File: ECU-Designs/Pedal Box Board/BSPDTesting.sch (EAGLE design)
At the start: 18 parts, among them X1 MINIFIT_5566-2

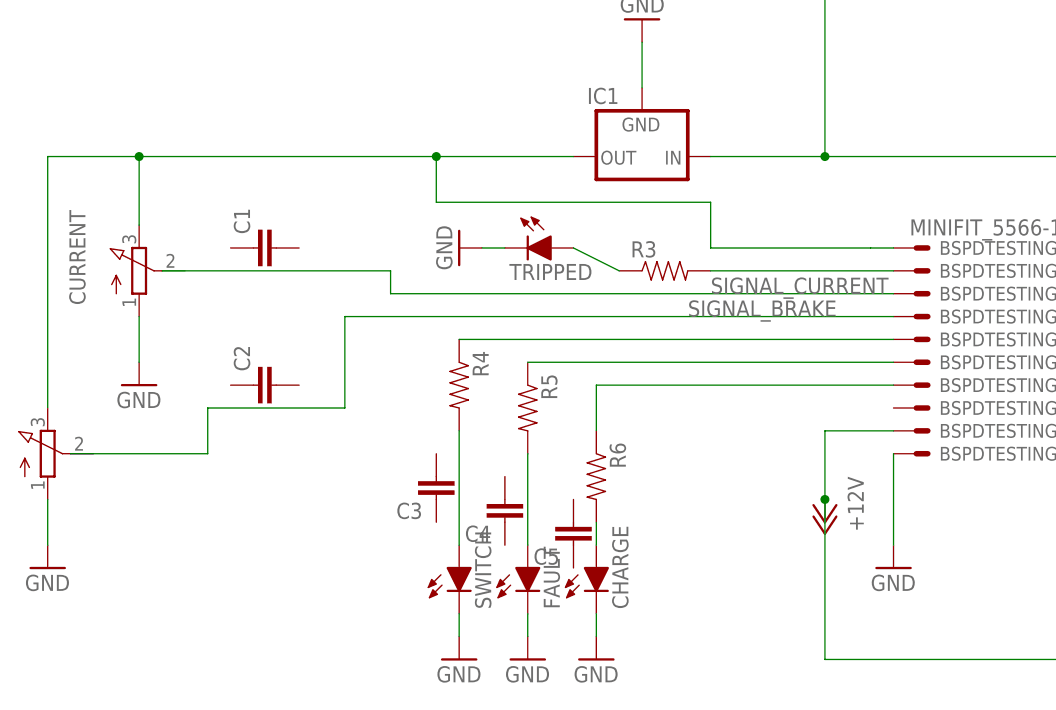
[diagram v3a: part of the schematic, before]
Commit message: Added Test Points to the library (usable with probes) updated board  to accomodate Test Probes.
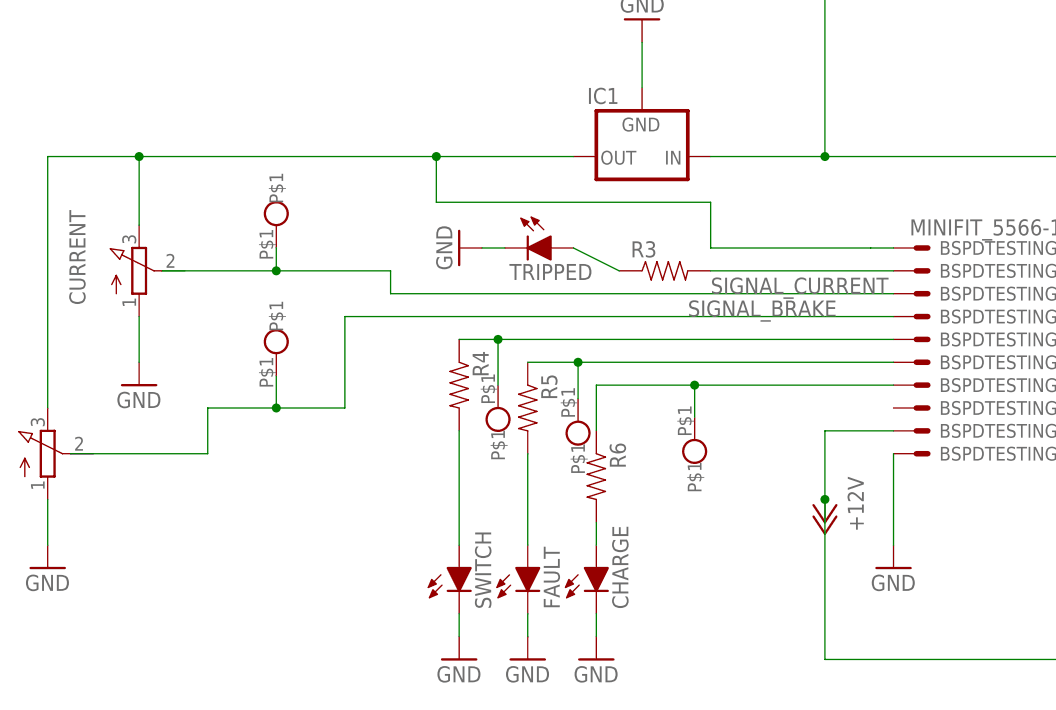
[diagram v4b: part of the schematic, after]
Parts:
- removed C1, C2, C3, C4, C5: (no value), HyTechDevices:CAPEZ
- added BRAKEPROBE, CURRENTPROBE, U$3, U$4, U$5: TEST_POINT_COMPACT_THM, HyTechDevices:TEST_POINT_COMPACT_THM
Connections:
- net N$10: now also U$4.P$1
- net N$14: now also U$5.P$1
- net N$9: now also U$3.P$1
- net SIGNAL_BRAKE: now also BRAKEPROBE.P$1
- net SIGNAL_CURRENT: now also CURRENTPROBE.P$1
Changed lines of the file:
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@@
 <setting verticaltext="up"/>
 </settings>
-<grid distance="0.1" unitdist="inch" unit="inch" style="lines" multiple="1" display="no" altdistance="0.01" altunitdist="inch" altunit="inch"/>
+<grid distance="0.01" unitdist="inch" unit="inch" style="lines" multiple="1" display="no" altdistance="0.01" altunitdist="inch" altunit="inch"/>
 <layers>
 <layer number="1" name="Top" color="4" fill="1" visible="no" active="no"/>
@@
 <part name="X1" library="HyTechDevices" deviceset="MINIFIT_5566-2" device=""/>
 <part name="GND9" library="supply1" deviceset="GND" device=""/>
-<part name="C1" library="HyTechDevices" deviceset="CAP" device="EZ"/>
-<part name="C2" library="HyTechDevices" deviceset="CAP" device="EZ"/>
-<part name="C3" library="HyTechDevices" deviceset="CAP" device="EZ"/>
-<part name="C4" library="HyTechDevices" deviceset="CAP" device="EZ"/>
-<part name="C5" library="HyTechDevices" deviceset="CAP" device="EZ"/>
+<part name="BRAKEPROBE" library="HyTechDevices" deviceset="TEST_POINT_COMPACT_THM" device=""/>
+<part name="CURRENTPROBE" library="HyTechDevices" deviceset="TEST_POINT_COMPACT_THM" device=""/>
+<part name="U$3" library="HyTechDevices" deviceset="TEST_POINT_COMPACT_THM" device=""/>
+<part name="U$4" library="HyTechDevices" deviceset="TEST_POINT_COMPACT_THM" device=""/>
+<part name="U$5" library="HyTechDevices" deviceset="TEST_POINT_COMPACT_THM" device=""/>
 </parts>
 <sheets>
@@
 <instance part="X1" gate="-1" x="96.52" y="104.14" rot="R90"/>
 <instance part="GND9" gate="1" x="96.52" y="99.06"/>
-<instance part="C1" gate="G$1" x="45.72" y="60.96" rot="R90"/>
-<instance part="C2" gate="G$1" x="45.72" y="45.72" rot="R90"/>
-<instance part="C3" gate="G$1" x="63.5" y="35.56" rot="R180"/>
-<instance part="C4" gate="G$1" x="71.12" y="33.02" rot="R180"/>
-<instance part="C5" gate="G$1" x="78.74" y="30.48" rot="R180"/>
+<instance part="BRAKEPROBE" gate="G$1" x="45.72" y="50.546" rot="R90"/>
+<instance part="CURRENTPROBE" gate="G$1" x="45.72" y="64.77" rot="R90"/>
+<instance part="U$3" gate="G$1" x="70.358" y="41.91" rot="R270"/>
+<instance part="U$4" gate="G$1" x="79.248" y="40.386" rot="R270"/>
+<instance part="U$5" gate="G$1" x="92.202" y="38.354" rot="R270"/>
 </instances>
 <busses>
@@
 <wire x1="22.86" y1="38.1" x2="38.1" y2="38.1" width="0.1524" layer="91"/>
 <wire x1="38.1" y1="38.1" x2="38.1" y2="43.18" width="0.1524" layer="91"/>
-<wire x1="53.34" y1="43.18" x2="38.1" y2="43.18" width="0.1524" layer="91"/>
+<wire x1="53.34" y1="43.18" x2="45.72" y2="43.18" width="0.1524" layer="91"/>
+<pinref part="BRAKEPROBE" gate="G$1" pin="P$1"/>
+<wire x1="45.72" y1="43.18" x2="38.1" y2="43.18" width="0.1524" layer="91"/>
+<wire x1="45.72" y1="46.736" x2="45.72" y2="43.18" width="0.1524" layer="91"/>
+<junction x="45.72" y="43.18"/>
 </segment>
 </net>
@@
 <pinref part="R4" gate="G$1" pin="1"/>
 <pinref part="BSPDTESTING" gate="-5" pin="S"/>
-<wire x1="66.04" y1="50.8" x2="114.3" y2="50.8" width="0.1524" layer="91"/>
+<wire x1="66.04" y1="50.8" x2="70.358" y2="50.8" width="0.1524" layer="91"/>
+<pinref part="U$3" gate="G$1" pin="P$1"/>
+<wire x1="70.358" y1="50.8" x2="114.3" y2="50.8" width="0.1524" layer="91"/>
+<wire x1="70.358" y1="45.72" x2="70.358" y2="50.8" width="0.1524" layer="91"/>
+<junction x="70.358" y="50.8"/>
 </segment>
 </net>
@@
 <pinref part="BSPDTESTING" gate="-6" pin="S"/>
 <pinref part="R5" gate="G$1" pin="1"/>
-<wire x1="114.3" y1="48.26" x2="73.66" y2="48.26" width="0.1524" layer="91"/>
+<wire x1="114.3" y1="48.26" x2="79.248" y2="48.26" width="0.1524" layer="91"/>
+<pinref part="U$4" gate="G$1" pin="P$1"/>
+<wire x1="79.248" y1="48.26" x2="73.66" y2="48.26" width="0.1524" layer="91"/>
+<wire x1="79.248" y1="44.196" x2="79.248" y2="48.26" width="0.1524" layer="91"/>
+<junction x="79.248" y="48.26"/>
 </segment>
 </net>
@@
 <segment>
 <pinref part="BSPDTESTING" gate="-7" pin="S"/>
-<wire x1="81.28" y1="45.72" x2="114.3" y2="45.72" width="0.1524" layer="91"/>
+<wire x1="81.28" y1="45.72" x2="92.202" y2="45.72" width="0.1524" layer="91"/>
 <pinref part="R6" gate="G$1" pin="1"/>
+<wire x1="92.202" y1="45.72" x2="114.3" y2="45.72" width="0.1524" layer="91"/>
 <wire x1="81.28" y1="45.72" x2="81.28" y2="40.64" width="0.1524" layer="91"/>
+<wire x1="92.202" y1="42.164" x2="92.202" y2="45.72" width="0.1524" layer="91"/>
+<junction x="92.202" y="45.72"/>
+<pinref part="U$5" gate="G$1" pin="P$1"/>
 </segment>
 </net>
@@
 <pinref part="BSPDTESTING" gate="-3" pin="S"/>
 <wire x1="114.3" y1="55.88" x2="58.42" y2="55.88" width="0.1524" layer="91"/>
-<wire x1="33.02" y1="58.42" x2="58.42" y2="58.42" width="0.1524" layer="91"/>
-</segment>
-</net>
+<wire x1="33.02" y1="58.42" x2="45.72" y2="58.42" width="0.1524" layer="91"/>
+<wire x1="45.72" y1="58.42" x2="58.42" y2="58.42" width="0.1524" layer="91"/>
+<junction x="45.72" y="58.42"/>
+<pinref part="CURRENTPROBE" gate="G$1" pin="P$1"/>
+<wire x1="45.72" y1="60.96" x2="45.72" y2="58.42" width="0.1524" layer="91"/>
+</segment>
+</net>

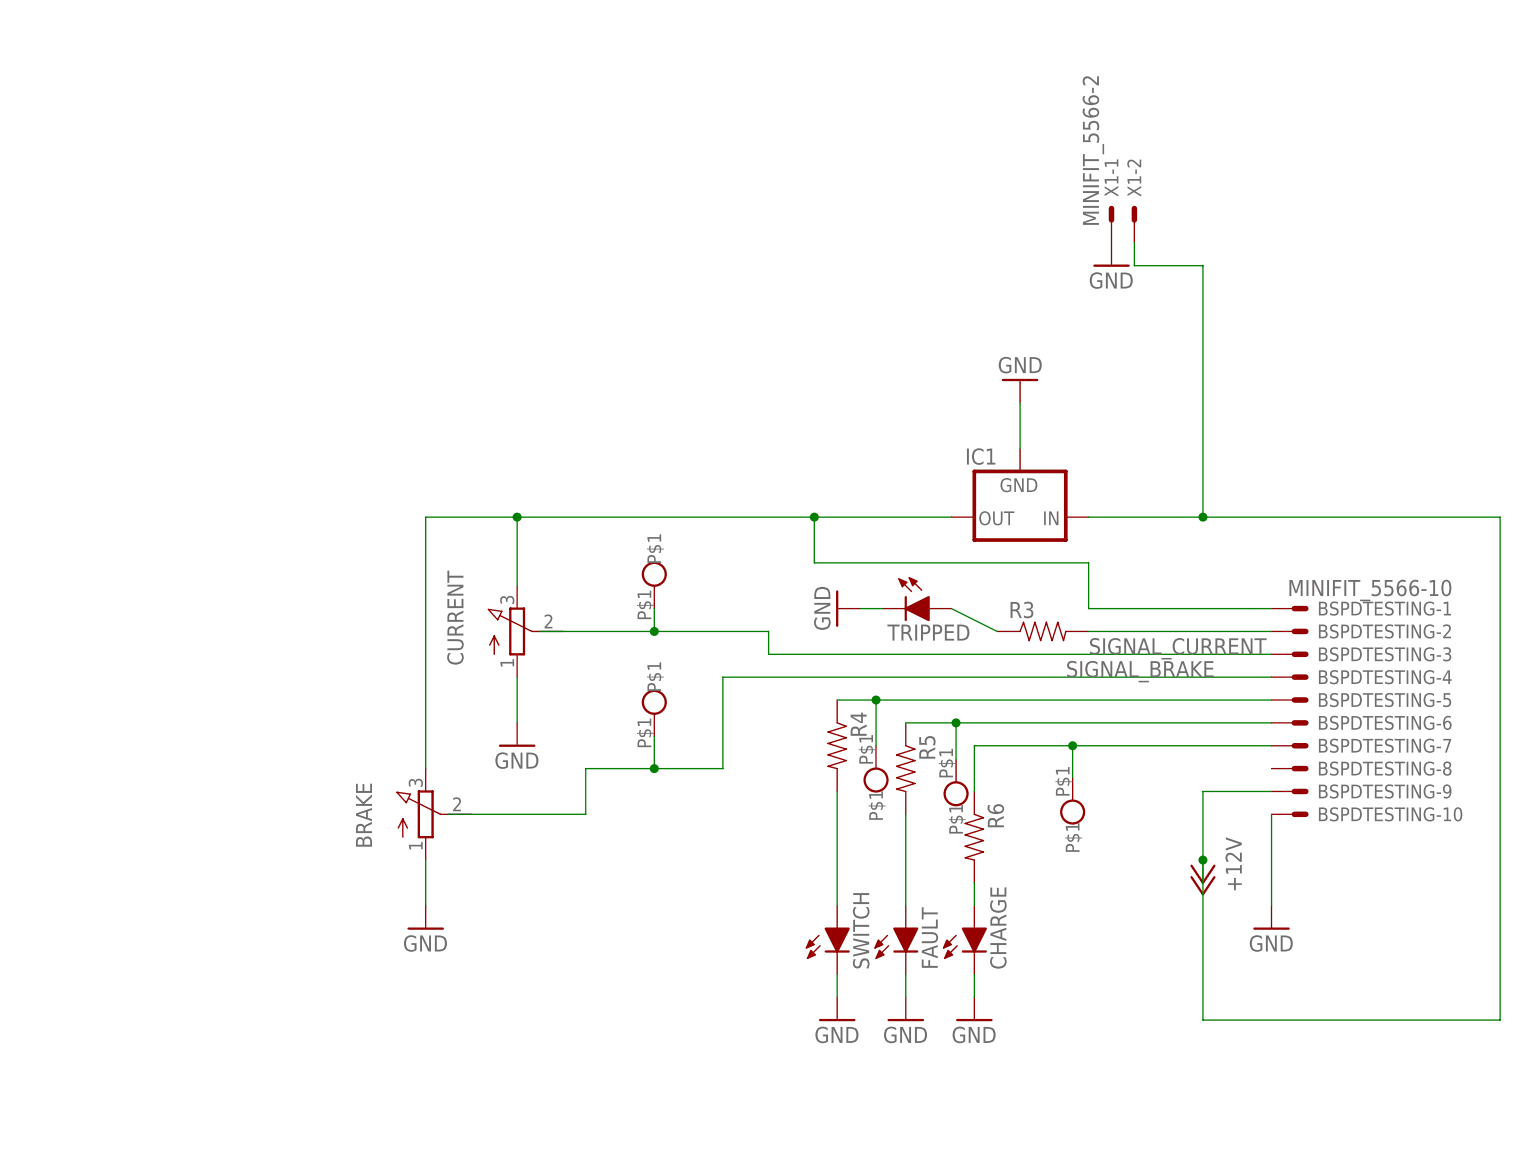
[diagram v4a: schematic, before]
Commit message: Added minifits to the signal wires and made a slight revision to the test point in the library
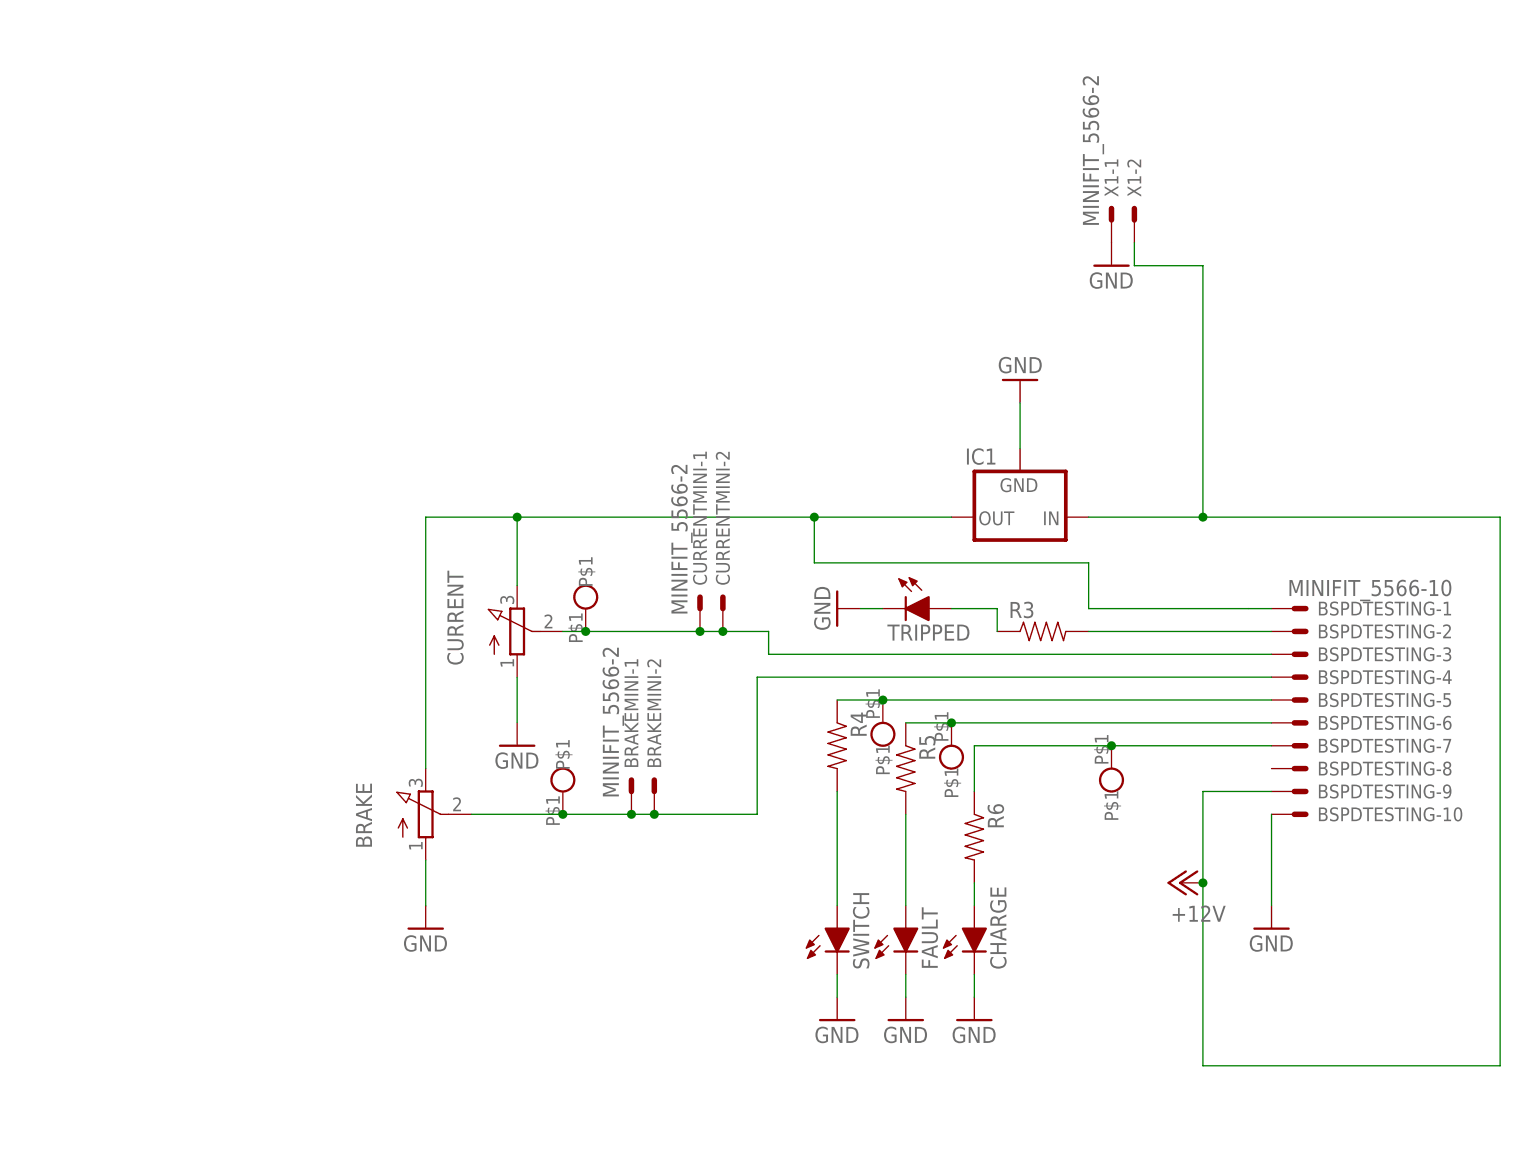
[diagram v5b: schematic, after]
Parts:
- removed BRAKEPROBE, CURRENTPROBE: TEST_POINT_COMPACT_THM, HyTechDevices:TEST_POINT_COMPACT_THM
- added BRAKEMINI, CURRENTMINI: MINIFIT_5566-2, HyTechDevices:MINIFIT_5566-2
- added U$1, U$2: TEST_POINT_COMPACT_THM, HyTechDevices:TEST_POINT_COMPACT_THM
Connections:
- removed net SIGNAL_BRAKE: BRAKEPROBE.P$1, BSPDTESTING-4.S
- removed net SIGNAL_CURRENT: BSPDTESTING-3.S, CURRENTPROBE.P$1
- new net N$11: BRAKE.S, BRAKEMINI-1.S, BRAKEMINI-2.S, BSPDTESTING-4.S, U$1.P$1
- new net N$12: BSPDTESTING-3.S, CURRENT.S, CURRENTMINI-1.S, CURRENTMINI-2.S, U$2.P$1
